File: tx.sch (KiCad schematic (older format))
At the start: 37 parts, among them T2 Transformer_1P_SS, U10 TLV2464CD, U11 SN74CBT3253

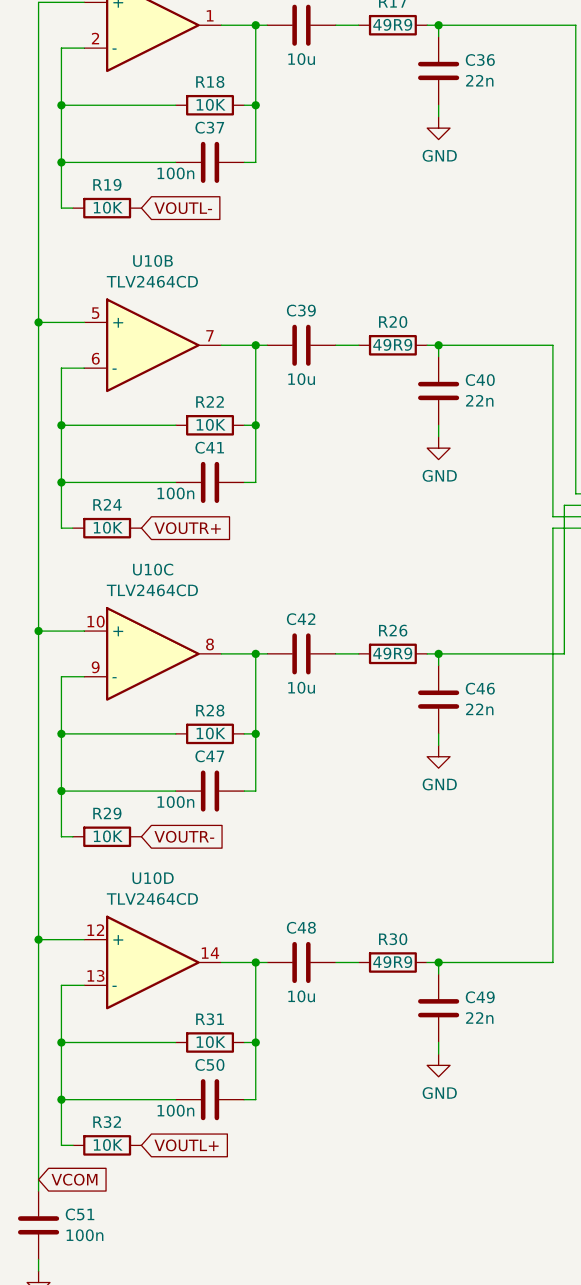
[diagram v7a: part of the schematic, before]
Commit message: Corrected wrong TX opamp capacitors values
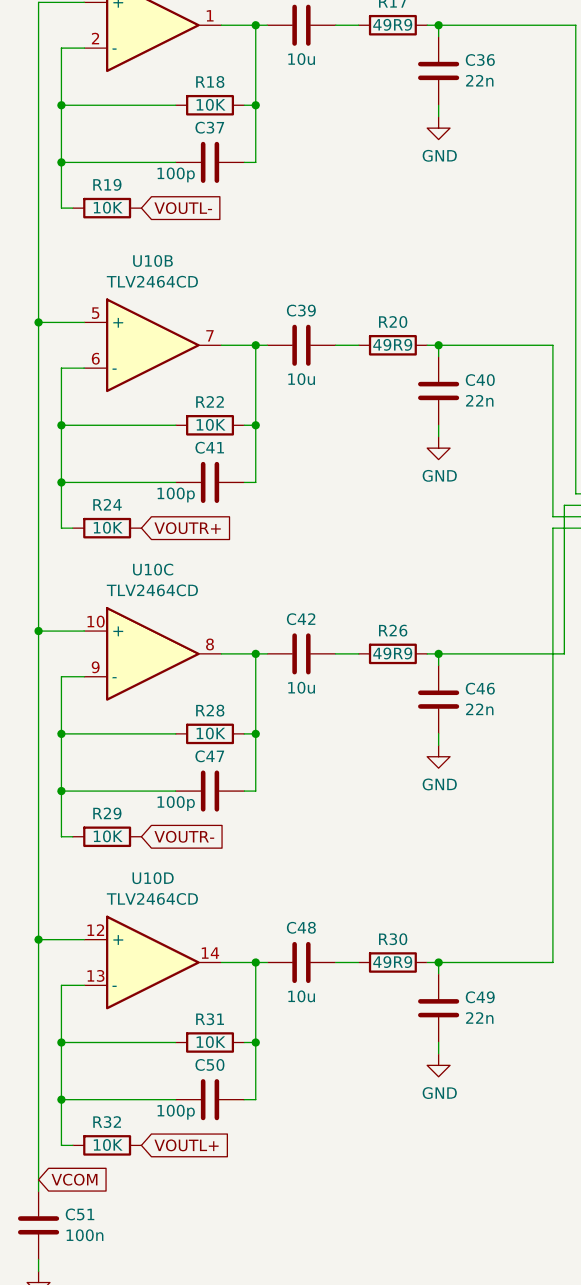
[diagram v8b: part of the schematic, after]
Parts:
- C37, C41, C47, C50: value 100n -> 100p
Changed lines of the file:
@@
 AR Path="/5EAFBA6A/5EB0EF48" Ref="C37"  Part="1"
 F 0 "C37" V 2325 2150 50  0000 C CNN
-F 1 "100n" V 2525 2000 50  0000 C CNN
+F 1 "100p" V 2525 2000 50  0000 C CNN
 F 2 "Capacitor_SMD:C_0603_1608Metric" H 2513 2000 50  0001 C CNN
 F 3 "~" H 2475 2150 50  0001 C CNN
@@
 AR Path="/5EAFBA6A/5EB0EF9C" Ref="C41"  Part="1"
 F 0 "C41" V 2325 3550 50  0000 C CNN
-F 1 "100n" V 2525 3400 50  0000 C CNN
+F 1 "100p" V 2525 3400 50  0000 C CNN
 F 2 "Capacitor_SMD:C_0603_1608Metric" H 2513 3400 50  0001 C CNN
 F 3 "~" H 2475 3550 50  0001 C CNN
@@
 AR Path="/5EAFBA6A/5EB0EFDE" Ref="C47"  Part="1"
 F 0 "C47" V 2325 4900 50  0000 C CNN
-F 1 "100n" V 2525 4750 50  0000 C CNN
+F 1 "100p" V 2525 4750 50  0000 C CNN
 F 2 "Capacitor_SMD:C_0603_1608Metric" H 2513 4750 50  0001 C CNN
 F 3 "~" H 2475 4900 50  0001 C CNN
@@
 AR Path="/5EAFBA6A/5EB0F020" Ref="C50"  Part="1"
 F 0 "C50" V 2325 6250 50  0000 C CNN
-F 1 "100n" V 2525 6100 50  0000 C CNN
+F 1 "100p" V 2525 6100 50  0000 C CNN
 F 2 "Capacitor_SMD:C_0603_1608Metric" H 2513 6100 50  0001 C CNN
 F 3 "~" H 2475 6250 50  0001 C CNN
